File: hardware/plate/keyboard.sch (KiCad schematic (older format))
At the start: 332 parts, among them J1 USB_C_Receptacle_USB2.0, J2 SWD, Q1 BSS138, Q2 BSS138, Q3 DTC123J, SW1 SW_Push, U1 USBLC6-2SC6, U2 AP2112K-3.3, U3 STM32F303RCTx, Y1 8MHz

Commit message: update mounting hole locations
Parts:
- removed BZ1: Buzzer, Buzzer_Beeper:Buzzer_Murata_PKMCS0909E4000-R1, symbol Device:Buzzer
- removed C1, C2: 1u, Capacitor_SMD:C_0603_1608Metric, symbol Device:C
- removed C10, C11, C12, C13, C14, C15, C16, C17, C18, C19, C20, C21, C22, C23, C24, C25, C27, C28, C29, C30, C32, C33, C34, C35, C36, C37, C38, C39, C6, C7, C8, C9: 100n, Capacitor_SMD:C_0603_1608Metric, symbol Device:C
- removed C26: 4u7, Capacitor_SMD:C_0603_1608Metric, symbol Device:C
- removed C3, C40: 10u, Capacitor_SMD:C_0603_1608Metric, symbol Device:C
- removed C4, C5: 22P, Capacitor_SMD:C_0603_1608Metric, symbol Device:C
- removed D1, D10, D11, D12, D13, D15, D17, D2, D20, D3, D4, D5, D6, D7, D8, D9: WS2812B, LED_SMD:LED_WS2812B_PLCC4_5.0x5.0mm_P3.2mm, symbol LED:WS2812B
- removed D14: LED, LED_SMD:LED_0603_1608Metric, symbol Device:LED
- removed D21, D22, D23, D25: SK6812-MINI-E, josh-led:SK8612-MINI-E, symbol josh-led:SK6812-MINI-E
- removed D24: 1N4148, Diode_SMD:D_SOD-123, symbol Device:D
- removed D_0, D_1, D_10, D_100, D_101, D_102, D_103, D_104, D_105, D_106, D_107, D_108, D_11, D_110, D_112, D_114, D_12, D_13, D_14, D_15, D_16, D_17, D_18, D_19, D_2, D_20, D_21, D_22, D_23, D_24, D_25, D_26, D_27, D_28, D_29, D_3, D_30, D_31, D_32, D_33, D_34, D_35, D_36, D_37, D_38, D_39, D_4, D_40, D_41, D_42, D_43, D_44, D_45, D_46, D_47, D_48, D_49, D_5, D_50, D_51, D_52, D_53, D_54, D_55, D_56, D_57, D_58, D_6, D_60, D_61, D_62, D_63, D_64, D_65, D_66, D_67, D_68, D_69, D_7, D_70, D_71, D_72, D_73, D_74, D_75, D_76, D_77, D_78, D_79, D_8, D_80, D_81, D_82, D_83, D_84, D_85, D_86, D_87, D_88, D_89, D_9, D_90, D_91, D_92, D_93, D_94, D_95, D_97, D_98, D_99: 1N4148, Diode_SMD:D_SOD-123, symbol Device:D_Small
- removed F1: 500mA, josh-passives-smt:Fuse_0805_2012Metric, symbol Device:Polyfuse
- removed FB1, FB2: 600R, josh-passives-smt:Ferrite_Bead_0603, symbol josh-passive:Ferrite_Bead_PWR
- removed J1: USB_C_Receptacle_USB2.0, josh-connectors:USB_C_U262-161N-4BVC11, symbol Connector:USB_C_Receptacle_USB2.0
- removed J2: SWD, josh-connectors:STM_4_PIN_THT_Staggered, symbol Connector:Conn_01x04_Male
- removed K_0, K_1, K_2, K_3: Encoder_MX, josh-keyboard:MX_KEYSWITCH_ENCODER, symbol Device:Rotary_Encoder_Switch
- removed K_10, K_105, K_106, K_107, K_108, K_109, K_11, K_113, K_114, K_115, K_12, K_13, K_14, K_15, K_16, K_17, K_18, K_19, K_20, K_21, K_22, K_23, K_24, K_25, K_26, K_27, K_28, K_29, K_30, K_31, K_32, K_33, K_34, K_35, K_36, K_38, K_39, K_4, K_41, K_42, K_43, K_45, K_46, K_47, K_48, K_49, K_5, K_50, K_51, K_52, K_53, K_54, K_55, K_56, K_58, K_59, K_6, K_60, K_61, K_62, K_64, K_65, K_66, K_67, K_68, K_69, K_7, K_70, K_71, K_72, K_73, K_74, K_76, K_77, K_79, K_8, K_80, K_81, K_83, K_84, K_85, K_86, K_87, K_88, K_89, K_9, K_90, K_91, K_92, K_94, K_95, K_96, K_97: KEYSW, josh-keyboard:MXOnly-1U-NoLED, symbol josh-keyboard:MX-NoLED
- removed K_100, K_101, K_111, K_99: KEYSW, josh-keyboard:MXOnly-1.25U-NoLED, symbol josh-keyboard:MX-NoLED
- removed K_102: KEYSW, josh-keyboard:MXOnly-6.25U-ReversedStabilizers-NoLED, symbol josh-keyboard:MX-NoLED
- removed K_103, K_104, K_44, K_57: KEYSW, josh-keyboard:MXOnly-1.5U-NoLED, symbol josh-keyboard:MX-NoLED
- removed K_110: KEYSW, josh-keyboard:MXOnly-2.75U-ReversedStabilizers-NoLED, symbol josh-keyboard:MX-NoLED
- removed K_112, K_75, K_82: KEYSW, josh-keyboard:MXOnly-2.25U-ReversedStabilizers-NoLED, symbol josh-keyboard:MX-NoLED
- removed K_37, K_40, K_78: KEYSW, josh-keyboard:MXOnly-2U-NoLED, symbol josh-keyboard:MX-NoLED
- removed K_63, K_93: KEYSW, josh-keyboard:MXOnly-1.75U-NoLED, symbol josh-keyboard:MX-NoLED
- removed K_98: KEYSW, josh-keyboard:MXOnly-2U-ReversedStabilizers-NoLED, symbol josh-keyboard:MX-NoLED
- removed LOGO4: BSILK, graphics:back_silk_v0, symbol Mechanical:MountingHole
- removed Q1, Q2: BSS138, Package_TO_SOT_SMD:SOT-23, symbol Transistor_FET:BSS138
- removed Q3: DTC123J, Package_TO_SOT_SMD:SOT-23, symbol Transistor_BJT:DTC123J
- removed R1, R2, R3, R4: 10K, Resistor_SMD:R_0603_1608Metric, symbol Device:R
- removed R10, R11, R7, R9: 1K5, Resistor_SMD:R_0603_1608Metric, symbol Device:R
- removed R5, R6: 5K1, Resistor_SMD:R_0603_1608Metric, symbol Device:R
- removed R8: 100K, Resistor_SMD:R_0603_1608Metric, symbol Device:R
- removed RN1, RN2, RN3, RN4: 10K, Resistor_SMD:R_Array_Convex_4x0603, symbol josh-passive:RN
- removed SW1: SW_Push, josh-buttons-switches:Panasonic_EVQPUL_EVQPUC, symbol Switch:SW_Push
- removed U1: USBLC6-2SC6, Package_TO_SOT_SMD:SOT-23-6, symbol josh-ic:USBLC6-2SC6
- removed U2: AP2112K-3.3, Package_TO_SOT_SMD:SOT-23-5, symbol Regulator_Linear:AP2112K-3.3
- removed U3: STM32F303RCTx, Package_QFP:LQFP-64_10x10mm_P0.5mm, symbol MCU_ST_STM32F3:STM32F303RCTx
- removed Y1: 8MHz, josh-oscillators:Crystal_SMD_3225-4Pin_3.2x2.5mm, symbol Device:Crystal_GND24
- H1, H10, H11, H12, H2, H3, H4, H5, H6, H7, H8, H9: value 3.5mm ID -> M2.5; footprint MountingHole:MountingHole_3.5mm -> MountingHole:MountingHole_2.7mm_M2.5
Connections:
- net labels removed: +3V3, +5V, BOOT0, BUZZER, ENC0_A, ENC0_A_DB, ENC0_B, ENC0_B_DB, ENC1_A, ENC1_A_DB, ENC1_B, ENC1_B_DB, ENC2_A, ENC2_A_DB, ENC2_B, ENC2_B_DB, ENC3_A, ENC3_A_DB, ENC3_B, ENC3_B_DB, GND, MCU_RST, SWDCLK, SWDIO, USB+, USB-, USB_D+, USB_D-, VBUS, XTAL_0, XTAL_1, col0, col1, col10, col11, col12, col13, col14, col15, col16, col17, col18, col19, col2, col3, col4, col5, col6, col7, col8, col9, nRST, row0, row1, row2, row3, row4, row5, status, underglow
- wire segments 846 -> 0
- no-connect marks 4 -> 0
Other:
- note removed: "3v3 -> 5v logic shift"
- note removed: "Bangers r us"
- note removed: "DFU / Reset"
- note removed: "Encoder Debouncing"
- note removed: "Keyboard Matrix"
- note removed: "Mounting Holes"
- note removed: "Place under space bar"
- note removed: "Programming"
- note removed: "Status"
- note removed: "Stopping \nERC Errors"
- note removed: "The Brains!"
- note removed: "USB / Power"
- note removed: "Underglow"

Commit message: mechanical changes
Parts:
- H1, H10, H11, H12, H2, H3, H4, H5, H6, H7, H8, H9: footprint MountingHole:MountingHole_2.7mm_M2.5 -> MountingHole:MountingHole_2.2mm_M2
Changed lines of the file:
@@
 F 0 "H1" H 14050 14446 50  0000 L CNN
 F 1 "M2.5" H 14050 14355 50  0000 L CNN
-F 2 "MountingHole:MountingHole_2.7mm_M2.5" H 13950 14400 50  0001 C CNN
+F 2 "MountingHole:MountingHole_2.2mm_M2" H 13950 14400 50  0001 C CNN
 F 3 "~" H 13950 14400 50  0001 C CNN
 F 4 "DNP" H 13950 14400 50  0001 C CNN "DNP"
@@
 F 0 "H2" H 14050 14646 50  0000 L CNN
 F 1 "M2.5" H 14050 14555 50  0000 L CNN
-F 2 "MountingHole:MountingHole_2.7mm_M2.5" H 13950 14600 50  0001 C CNN
+F 2 "MountingHole:MountingHole_2.2mm_M2" H 13950 14600 50  0001 C CNN
 F 3 "~" H 13950 14600 50  0001 C CNN
 F 4 "DNP" H 13950 14600 50  0001 C CNN "DNP"
@@
 F 0 "H3" H 14050 14846 50  0000 L CNN
 F 1 "M2.5" H 14050 14755 50  0000 L CNN
-F 2 "MountingHole:MountingHole_2.7mm_M2.5" H 13950 14800 50  0001 C CNN
+F 2 "MountingHole:MountingHole_2.2mm_M2" H 13950 14800 50  0001 C CNN
 F 3 "~" H 13950 14800 50  0001 C CNN
 F 4 "DNP" H 13950 14800 50  0001 C CNN "DNP"
@@
 F 0 "H4" H 14050 15046 50  0000 L CNN
 F 1 "M2.5" H 14050 14955 50  0000 L CNN
-F 2 "MountingHole:MountingHole_2.7mm_M2.5" H 13950 15000 50  0001 C CNN
+F 2 "MountingHole:MountingHole_2.2mm_M2" H 13950 15000 50  0001 C CNN
 F 3 "~" H 13950 15000 50  0001 C CNN
 F 4 "DNP" H 13950 15000 50  0001 C CNN "DNP"
@@
 F 0 "H5" H 14050 15246 50  0000 L CNN
 F 1 "M2.5" H 14050 15155 50  0000 L CNN
-F 2 "MountingHole:MountingHole_2.7mm_M2.5" H 13950 15200 50  0001 C CNN
+F 2 "MountingHole:MountingHole_2.2mm_M2" H 13950 15200 50  0001 C CNN
 F 3 "~" H 13950 15200 50  0001 C CNN
 F 4 "DNP" H 13950 15200 50  0001 C CNN "DNP"
@@
 F 0 "H6" H 14050 15446 50  0000 L CNN
 F 1 "M2.5" H 14050 15355 50  0000 L CNN
-F 2 "MountingHole:MountingHole_2.7mm_M2.5" H 13950 15400 50  0001 C CNN
+F 2 "MountingHole:MountingHole_2.2mm_M2" H 13950 15400 50  0001 C CNN
 F 3 "~" H 13950 15400 50  0001 C CNN
 F 4 "DNP" H 13950 15400 50  0001 C CNN "DNP"
@@
 F 0 "H12" H 14650 15446 50  0000 L CNN
 F 1 "M2.5" H 14650 15355 50  0000 L CNN
-F 2 "MountingHole:MountingHole_2.7mm_M2.5" H 14550 15400 50  0001 C CNN
+F 2 "MountingHole:MountingHole_2.2mm_M2" H 14550 15400 50  0001 C CNN
 F 3 "~" H 14550 15400 50  0001 C CNN
 F 4 "DNP" H 14550 15400 50  0001 C CNN "DNP"
@@
 F 0 "H11" H 14650 15246 50  0000 L CNN
 F 1 "M2.5" H 14650 15155 50  0000 L CNN
-F 2 "MountingHole:MountingHole_2.7mm_M2.5" H 14550 15200 50  0001 C CNN
+F 2 "MountingHole:MountingHole_2.2mm_M2" H 14550 15200 50  0001 C CNN
 F 3 "~" H 14550 15200 50  0001 C CNN
 F 4 "DNP" H 14550 15200 50  0001 C CNN "DNP"
@@
 F 0 "H10" H 14650 15046 50  0000 L CNN
 F 1 "M2.5" H 14650 14955 50  0000 L CNN
-F 2 "MountingHole:MountingHole_2.7mm_M2.5" H 14550 15000 50  0001 C CNN
+F 2 "MountingHole:MountingHole_2.2mm_M2" H 14550 15000 50  0001 C CNN
 F 3 "~" H 14550 15000 50  0001 C CNN
 F 4 "DNP" H 14550 15000 50  0001 C CNN "DNP"
@@
 F 0 "H9" H 14650 14846 50  0000 L CNN
 F 1 "M2.5" H 14650 14755 50  0000 L CNN
-F 2 "MountingHole:MountingHole_2.7mm_M2.5" H 14550 14800 50  0001 C CNN
+F 2 "MountingHole:MountingHole_2.2mm_M2" H 14550 14800 50  0001 C CNN
 F 3 "~" H 14550 14800 50  0001 C CNN
 F 4 "DNP" H 14550 14800 50  0001 C CNN "DNP"
@@
 F 0 "H8" H 14650 14646 50  0000 L CNN
 F 1 "M2.5" H 14650 14555 50  0000 L CNN
-F 2 "MountingHole:MountingHole_2.7mm_M2.5" H 14550 14600 50  0001 C CNN
+F 2 "MountingHole:MountingHole_2.2mm_M2" H 14550 14600 50  0001 C CNN
 F 3 "~" H 14550 14600 50  0001 C CNN
 F 4 "DNP" H 14550 14600 50  0001 C CNN "DNP"
@@
 F 0 "H7" H 14650 14446 50  0000 L CNN
 F 1 "M2.5" H 14650 14355 50  0000 L CNN
-F 2 "MountingHole:MountingHole_2.7mm_M2.5" H 14550 14400 50  0001 C CNN
+F 2 "MountingHole:MountingHole_2.2mm_M2" H 14550 14400 50  0001 C CNN
 F 3 "~" H 14550 14400 50  0001 C CNN
 F 4 "DNP" H 14550 14400 50  0001 C CNN "DNP"

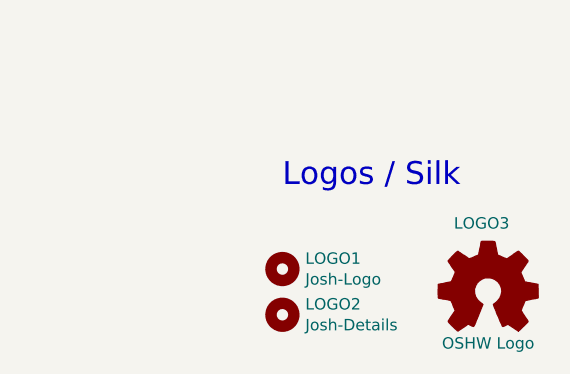
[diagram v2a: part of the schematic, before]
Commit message: add split backspace
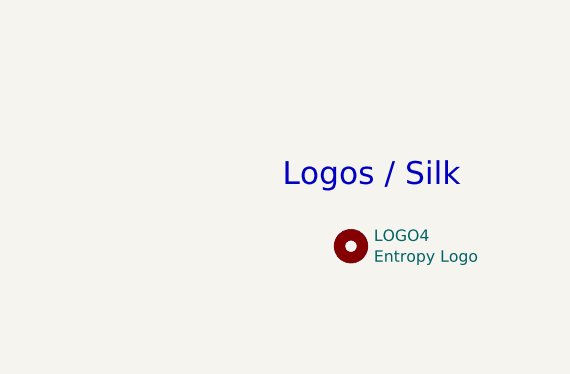
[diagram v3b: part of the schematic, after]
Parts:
- removed LOGO1: Josh-Logo, josh-logos:josh-johnson-logo-17x3, symbol Mechanical:MountingHole
- removed LOGO2: Josh-Details, josh-logos:josh-details, symbol Mechanical:MountingHole
- removed LOGO3: OSHW Logo, josh-logos:OSHW_Logo_3.6x3.6_F.Mask, symbol Graphic:Logo_Open_Hardware_Small
- added LOGO4: Entropy Logo, graphics:back_silk_v0, symbol Mechanical:MountingHole
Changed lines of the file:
@@
 Comment4 ""
 $EndDescr
-$Comp
-L Graphic:Logo_Open_Hardware_Small LOGO?
-U 1 1 619339EC
-P 17450 15700
-AR Path="/618A4248/619339EC" Ref="LOGO?"  Part="1"
-AR Path="/619339EC" Ref="LOGO3"  Part="1"
-F 0 "LOGO3" H 17300 16000 50  0000 L CNN
-F 1 "OSHW Logo" H 17450 15475 50  0000 C CNN
-F 2 "josh-logos:OSHW_Logo_3.6x3.6_F.Mask" H 17450 15700 50  0001 C CNN
-F 3 "~" H 17450 15700 50  0001 C CNN
-F 4 "DNP" H 17450 15700 50  0001 C CNN "DNP"
-	1    17450 15700
-	1    0    0    -1
-$EndComp
-$Comp
-L Mechanical:MountingHole LOGO?
-U 1 1 619339F3
-P 16550 15800
-AR Path="/618A4248/619339F3" Ref="LOGO?"  Part="1"
-AR Path="/619339F3" Ref="LOGO2"  Part="1"
-F 0 "LOGO2" H 16650 15846 50  0000 L CNN
-F 1 "Josh-Details" H 16650 15755 50  0000 L CNN
-F 2 "josh-logos:josh-details" H 16550 15800 50  0001 C CNN
-F 3 "~" H 16550 15800 50  0001 C CNN
-F 4 "DNP" H 16550 15800 50  0001 C CNN "DNP"
-	1    16550 15800
-	1    0    0    -1
-$EndComp
-$Comp
-L Mechanical:MountingHole LOGO?
-U 1 1 619339FA
-P 16550 15600
-AR Path="/618A4248/619339FA" Ref="LOGO?"  Part="1"
-AR Path="/619339FA" Ref="LOGO1"  Part="1"
-F 0 "LOGO1" H 16650 15646 50  0000 L CNN
-F 1 "Josh-Logo" H 16650 15555 50  0000 L CNN
-F 2 "josh-logos:josh-johnson-logo-17x3" H 16550 15600 50  0001 C CNN
-F 3 "~" H 16550 15600 50  0001 C CNN
-F 4 "DNP" H 16550 15600 50  0001 C CNN "DNP"
-	1    16550 15600
-	1    0    0    -1
-$EndComp
 Text Notes 16550 15250 0    100  ~ 0
 Logos / Silk
@@
 	1    0    0    -1
 $EndComp
+$Comp
+L Mechanical:MountingHole LOGO?
+U 1 1 5EEF2CEE
+P 16850 15500
+AR Path="/618A4248/5EEF2CEE" Ref="LOGO?"  Part="1"
+AR Path="/5EEF2CEE" Ref="LOGO4"  Part="1"
+F 0 "LOGO4" H 16950 15546 50  0000 L CNN
+F 1 "Entropy Logo" H 16950 15455 50  0000 L CNN
+F 2 "graphics:back_silk_v0" H 16850 15500 50  0001 C CNN
+F 3 "~" H 16850 15500 50  0001 C CNN
+F 4 "DNP" H 16850 15500 50  0001 C CNN "DNP"
+	1    16850 15500
+	1    0    0    -1
+$EndComp
